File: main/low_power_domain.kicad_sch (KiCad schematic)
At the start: 36 parts, among them IC1 STM32U073CCU6, IC2 IC_TEXAS_TPS62743YFPR, IC3 IC_TEXAS_TPS62743YFPR, IC4 PAM8302AASCR, U4 TMF8806, X1 XTAL_ABRACON_ABS07-32.768KHZ-T

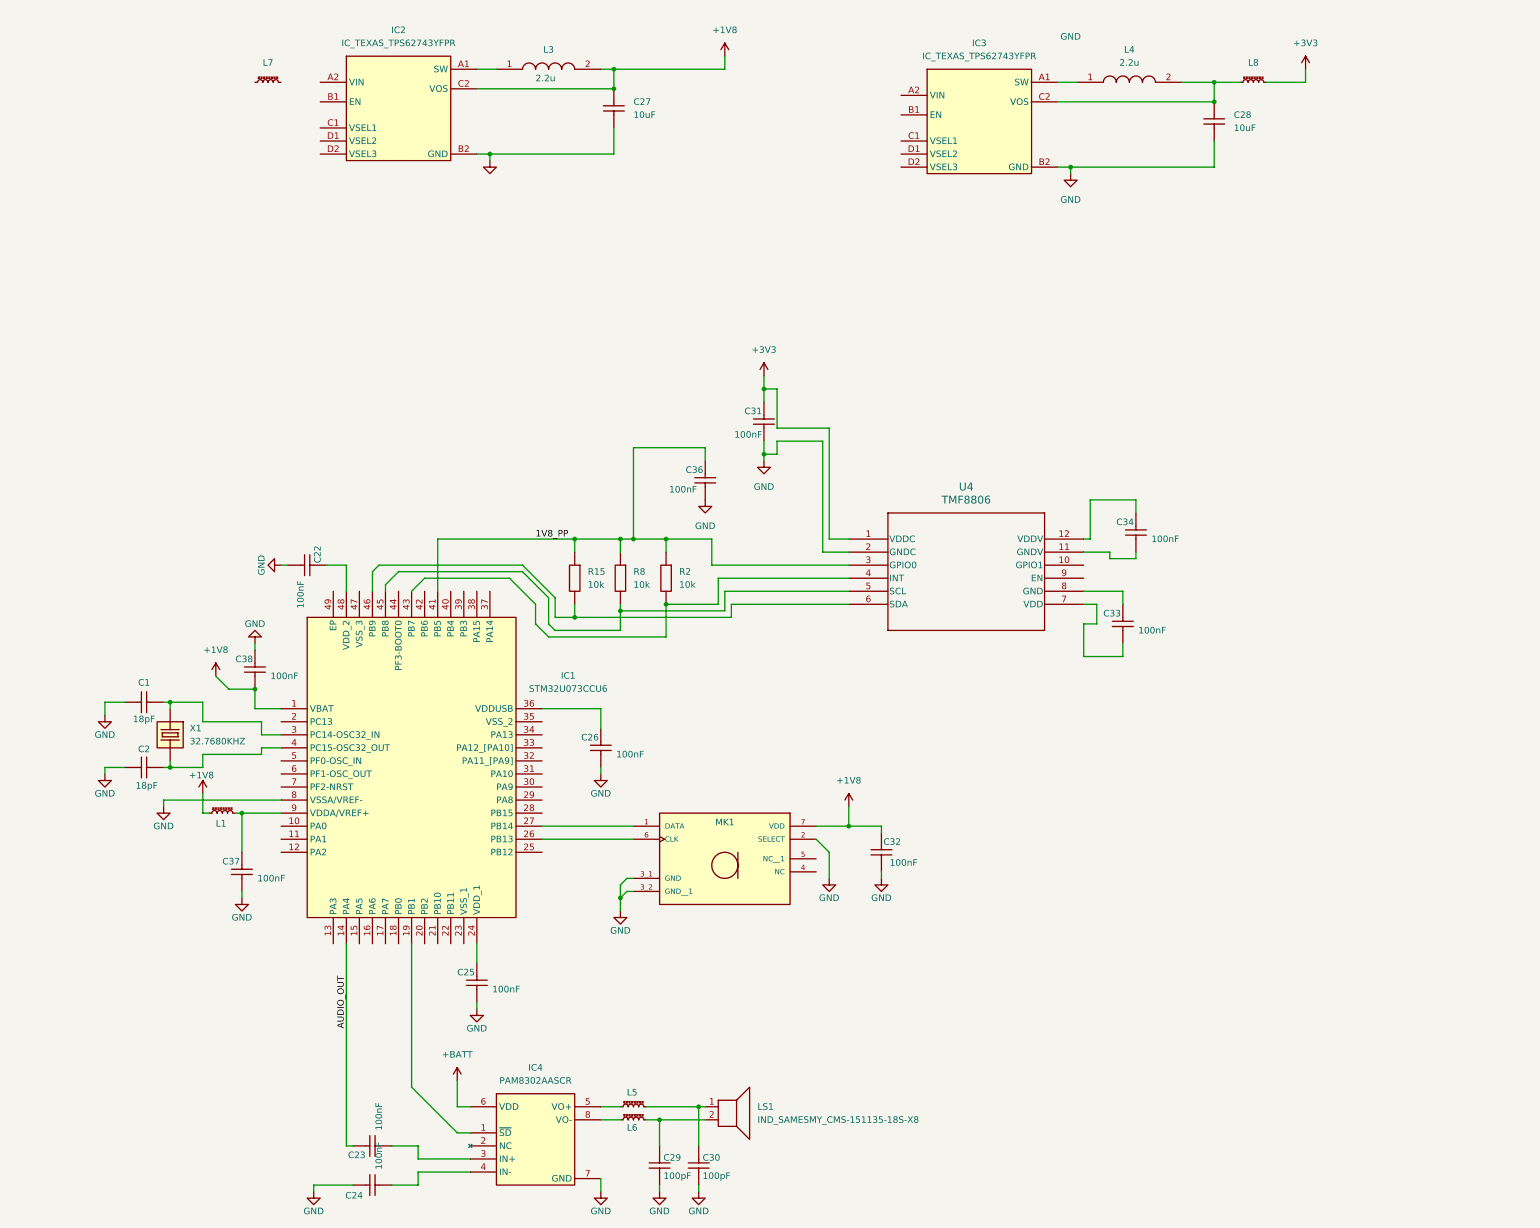
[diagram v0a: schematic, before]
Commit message: last commit with pi-pico still on
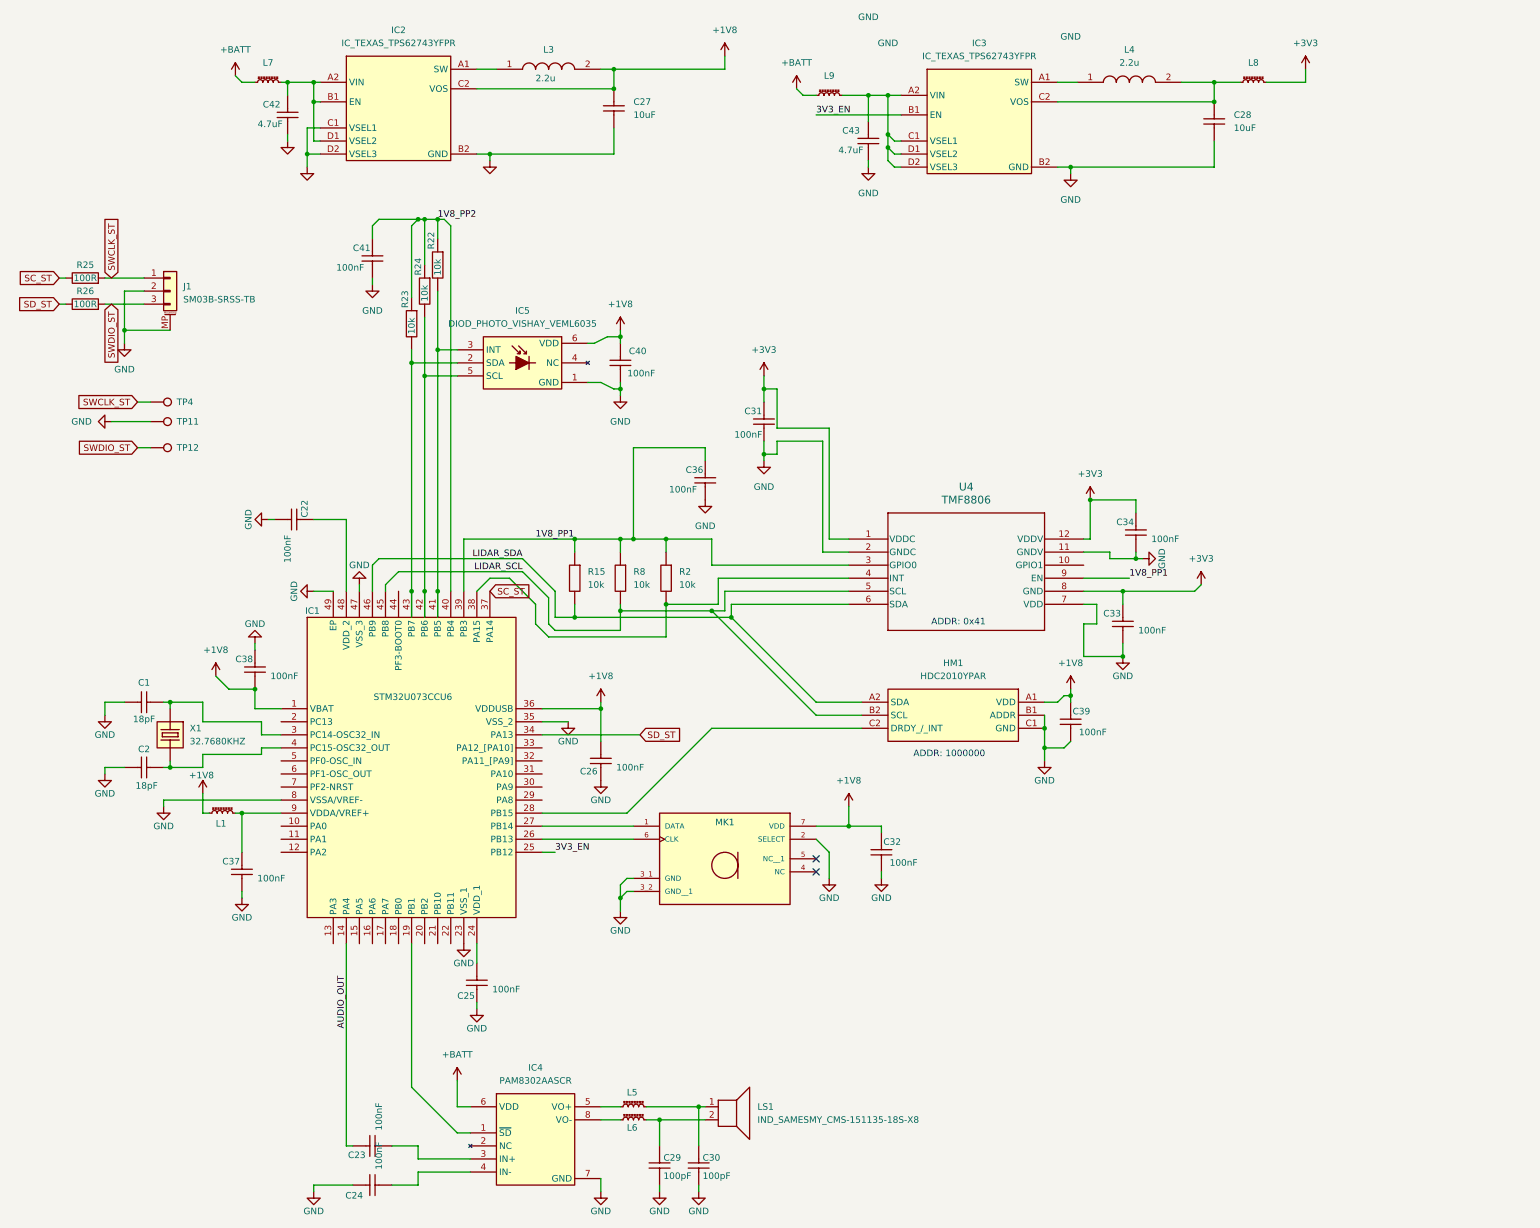
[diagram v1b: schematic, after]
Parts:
- added C39, C40, C41: 100NF_0201_10V_X7R, smv_footprints:C_0201_0603Metric, symbol smv_capacitors:100NF_0201_10V_X7R
- added C42, C43: 4.7UF 0402 10V X7R, smv_footprints:C_0402_1005Metric, symbol smv_capacitors:4.7UF_0402_10V_X7R
- added HM1: HDC2010YPAR, smv_footprints:IC_TEXAS_HDC2010YPAR, symbol IC_TEXAS_HDC2010YPAR:HDC2010YPAR
- added IC5: DIOD_PHOTO_VISHAY_VEML6035, smv_footprints:DIOD_PHOTO_VISHAY_VEML6035, symbol smv_diodes:DIOD_PHOTO_VISHAY_VEML6035
- added J1: SM03B-SRSS-TB, Connector_JST:JST_SH_SM03B-SRSS-TB_1x03-1MP_P1.00mm_Horizontal, symbol Connector_Generic_MountingPin:Conn_01x03_MountingPin
- added L9: INDC_BEAD_BLM18AG601SN1D, Inductor_SMD:L_0603_1608Metric, symbol smv_inductors:INDC_BEAD_BLM18AG601SN1D
- added R22, R23, R24: 10K 0402, smv_footprints:R_0402_1005Metric, symbol smv_resistors:10K 0402
- added R25, R26: 100R, Resistor_SMD:R_0201_0603Metric, symbol Device:R
- added TP11, TP12, TP4: TestPoint, TestPoint:TestPoint_Pad_1.5x1.5mm, symbol Connector:TestPoint
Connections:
- net +1V8: now also C26.1, IC1.36 (VDDUSB), C39.1, C40.1, HM1.A1 (VDD), IC5.6 (VDD)
- net +3V3: now also C33.1, C34.1, U4.12 (VDDV), U4.8 (GND)
- net +BATT: now also L7.1, L9.1
- net GND: now also C33.2, C34.2, IC1.23 (VSS_1), IC1.35 (VSS_2), IC1.47 (VSS_3), IC1.49 (EP), IC2.C1 (VSEL1), IC2.D2 (VSEL3), U4.11 (GNDV), U4.7 (VDD), C39.2, C40.2, C41.2, C42.2, C43.2, HM1.B1 (ADDR), HM1.C1 (GND), IC5.1 (GND), J1.2 (Pin_2), J1.MP (MountPin), TP11.1
- net 3V3_EN: now reaches IC1.25 (PB12)
- net 3V3_EN: now also IC3.B1 (EN)
- net at IC1.28 (PB15): now also HM1.C2 (DRDY_/_INT)
- net SD_ST: now reaches IC1.34 (PA13)
- net SD_ST: now also R26.1
- net SC_ST: now reaches IC1.37 (PA14)
- net SC_ST: now also R25.1
- net at IC1.38 (PA15): now also R2.1, U4.4 (INT)
- net 1V8_PP1: now reaches IC1.39 (PB3)
- net 1V8_PP1: now also C36.1, R15.2, R2.2, R8.2, U4.3 (GPIO0), U4.9 (EN)
- net 1V8_PP2: now reaches IC1.40 (PB4)
- net 1V8_PP2: now also C41.1, R22.2, R23.2, R24.2
- net at IC1.42 (PB6): now also IC5.5 (SCL), R24.1
- net LIDAR_SCL: now reaches IC1.45 (PB8), R8.1, U4.5 (SCL)
- net LIDAR_SCL: now also HM1.B2 (SCL)
- net LIDAR_SDA: now reaches IC1.46 (PB9), R15.1, U4.6 (SDA)
- net LIDAR_SDA: now also HM1.A2 (SDA)
- net at IC3.A2 (VIN): now also IC3.C1 (VSEL1), IC3.D1 (VSEL2), IC3.D2 (VSEL3), C43.1, L9.2
- net at IC2.A2 (VIN): now also IC2.B1 (EN), IC2.D1 (VSEL2), L7.2, C42.1
- removed net 1V8_PP: C36.1, IC1.41 (PB5), R15.2, R2.2, R8.2, U4.3 (GPIO0)
- new net: IC1.43 (PB7), IC5.2 (SDA), R23.1
- new net: IC1.41 (PB5), IC5.3 (INT), R22.1
- new net SWCLK_ST: J1.1 (Pin_1), R25.2, TP4.1
- new net SWDIO_ST: J1.3 (Pin_3), R26.2, TP12.1
- no-connect marks 0 -> 2
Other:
- note added: "ADDR: 0x41"
- note added: "ADDR: 1000000"
- moved on the sheet: C22, C26

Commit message: added leds and removed pico, changed outline
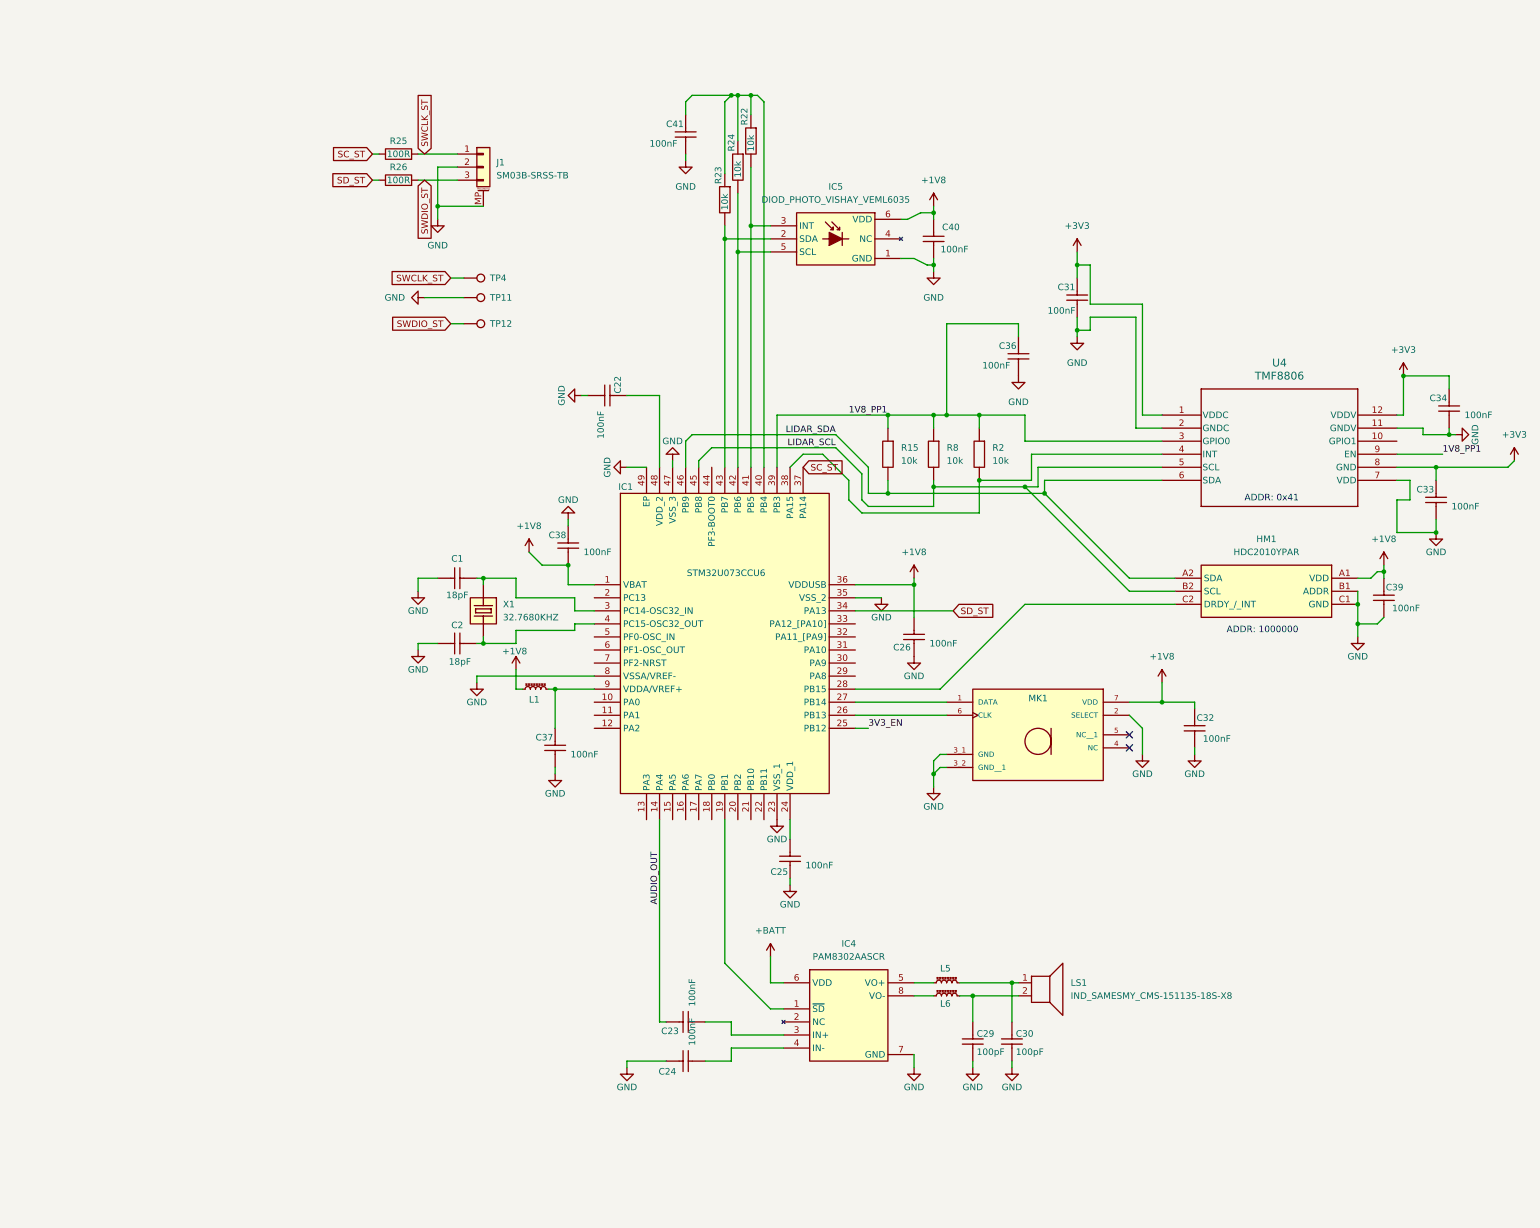
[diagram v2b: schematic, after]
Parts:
- removed C27, C28: 10UF_0805_16V_X7R, smv_footprints:C_0805_2012Metric, symbol smv_capacitors:10UF_0805_16V_X7R
- removed C42, C43: 4.7UF 0402 10V X7R, smv_footprints:C_0402_1005Metric, symbol smv_capacitors:4.7UF_0402_10V_X7R
- removed IC2, IC3: IC_TEXAS_TPS62743YFPR, smv_footprints:BGA8C40P2X4_87X156X53, symbol smv_ic:IC_TEXAS_TPS62743YFPR
- removed L3, L4: 2.2u, smv_footprints:IND_MURATA_DFE201610P-2R2M=P2, symbol smv_inductors:IND_MURATA_DFE201610P-2R2M=P2
- removed L7, L8, L9: INDC_BEAD_BLM18AG601SN1D, Inductor_SMD:L_0603_1608Metric, symbol smv_inductors:INDC_BEAD_BLM18AG601SN1D
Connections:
- net 1V8_PP2: no longer names the net of C41.1, IC1.40 (PB4), R22.2, R23.2, R24.2
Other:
- moved on the sheet: C1, C2, C22, C23, C24, C25, C26, C29, C30, C31, C32, C33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
